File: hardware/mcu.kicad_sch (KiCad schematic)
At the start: 2 parts, among them U1 NUCLEO-H503RB, U2 SN74LVC1T45DBV

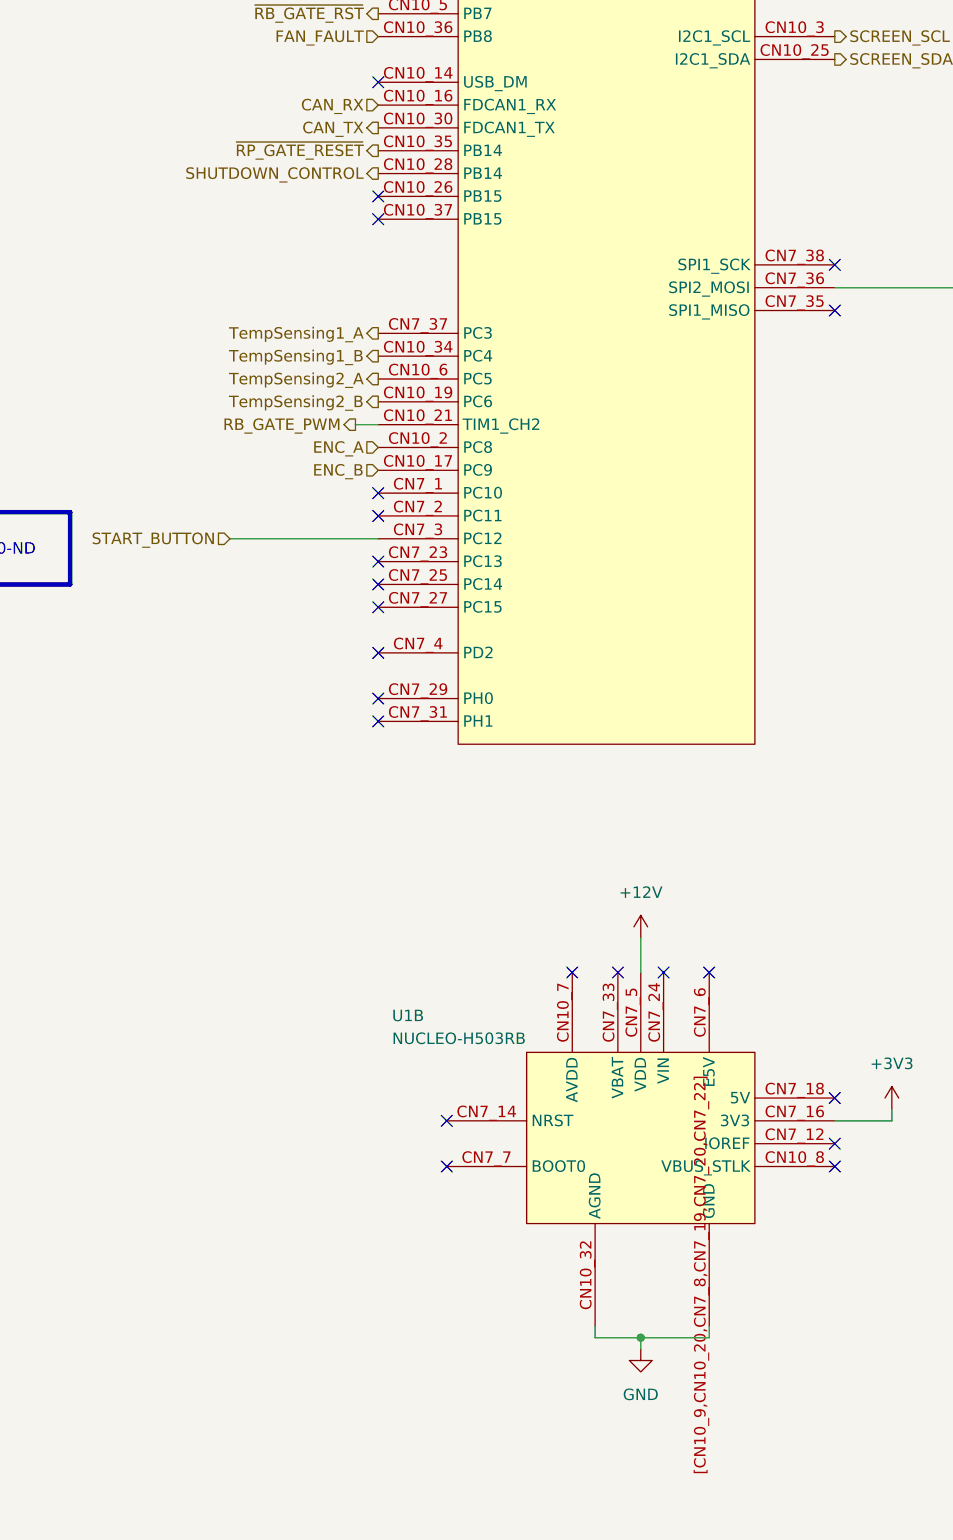
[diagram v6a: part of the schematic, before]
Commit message: completed main board schematic
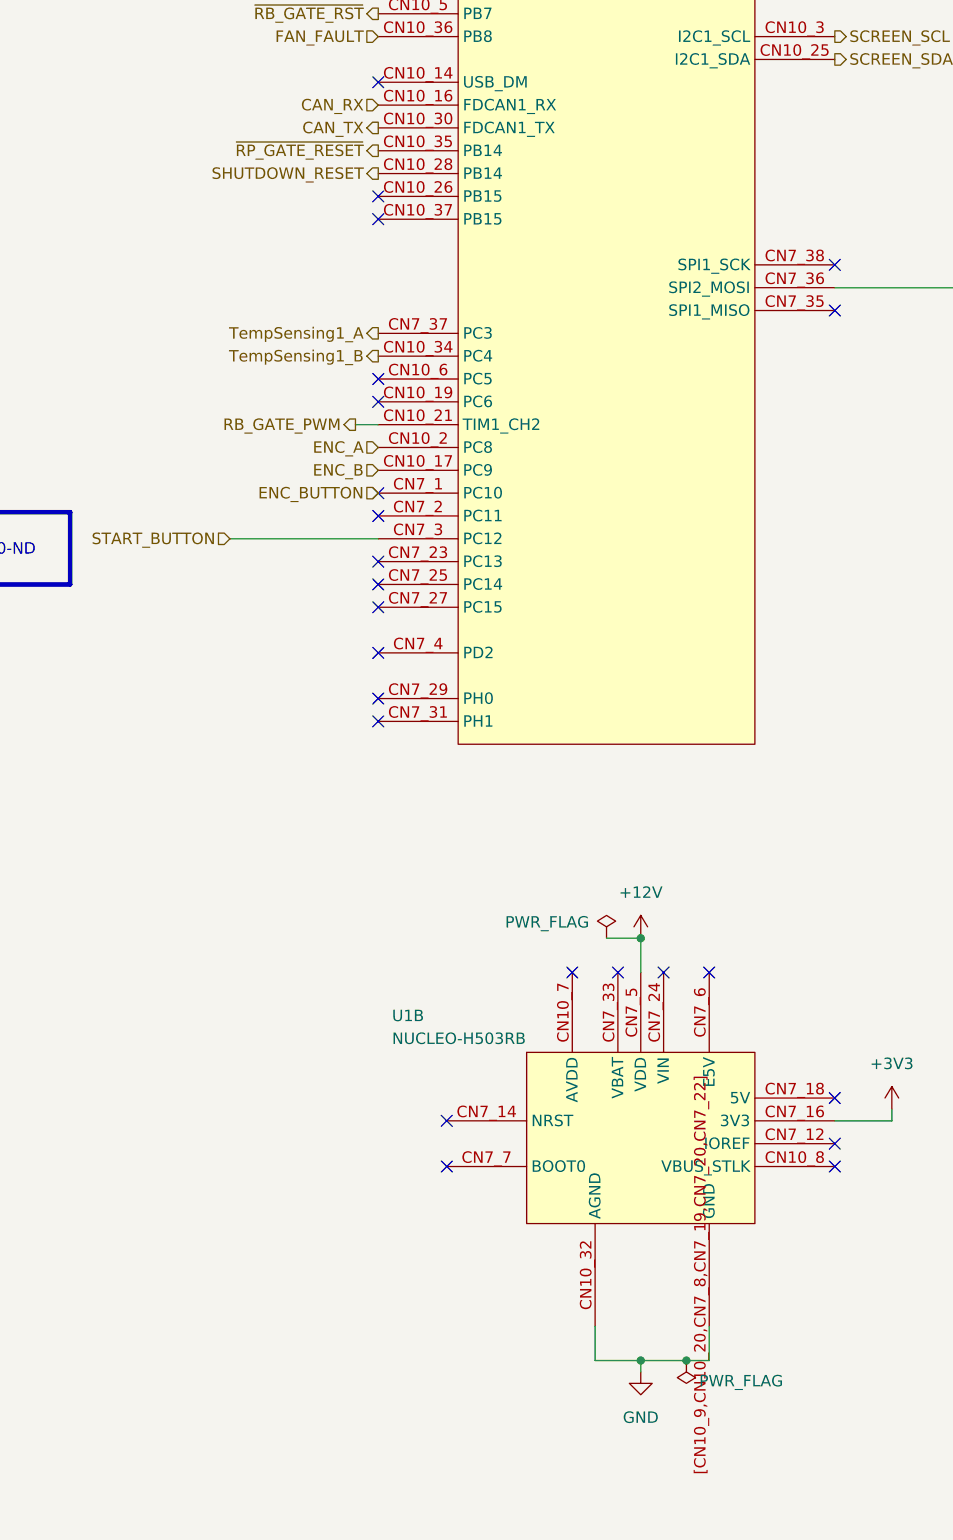
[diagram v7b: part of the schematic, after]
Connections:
- net ENC_BUTTON: now reaches U1.CN7_1 (PC10)
- net SHUTDOWN_CONTROL renamed SHUTDOWN_RESET
- net TempSensing2_A: no longer names the net of U1.CN10_6 (PC5)
- net TempSensing2_B: no longer names the net of U1.CN10_19 (PC6)
- no-connect marks 28 -> 30

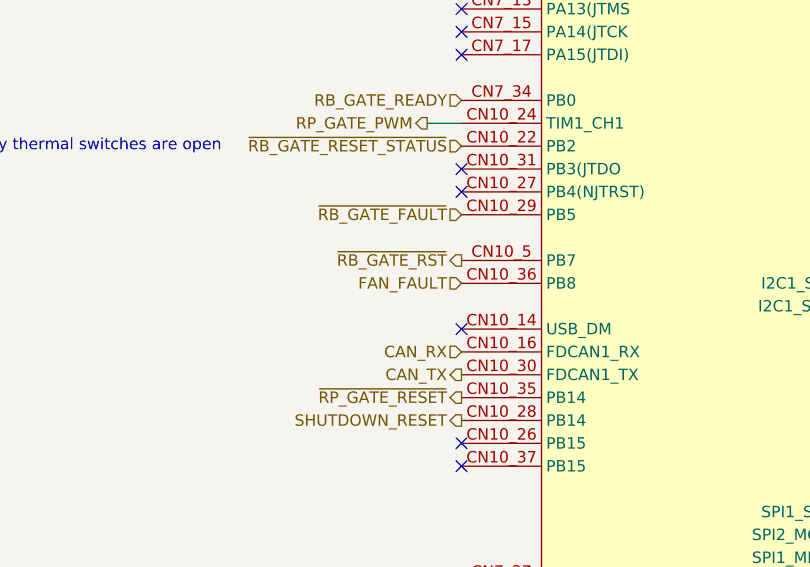
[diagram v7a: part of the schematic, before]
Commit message: initial layout, power traces remain
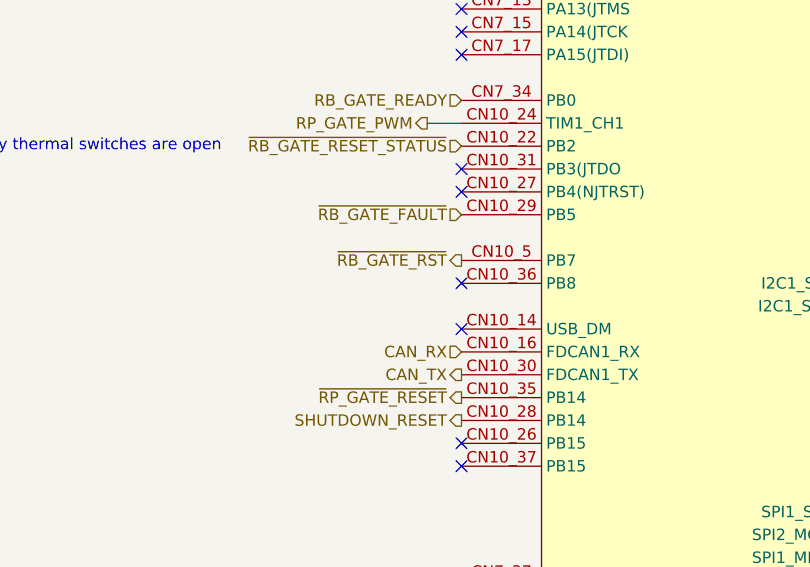
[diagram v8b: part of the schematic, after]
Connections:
- net FAN_FAULT: no longer names the net of U1.CN10_36 (PB8)
- no-connect marks 30 -> 31
